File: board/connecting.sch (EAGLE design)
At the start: 14 parts, among them J1 22-05-7038-03, J2 22-05-7038-03, J3 22-05-7038-03, K1 G5L, T1 BC817, X1 External input

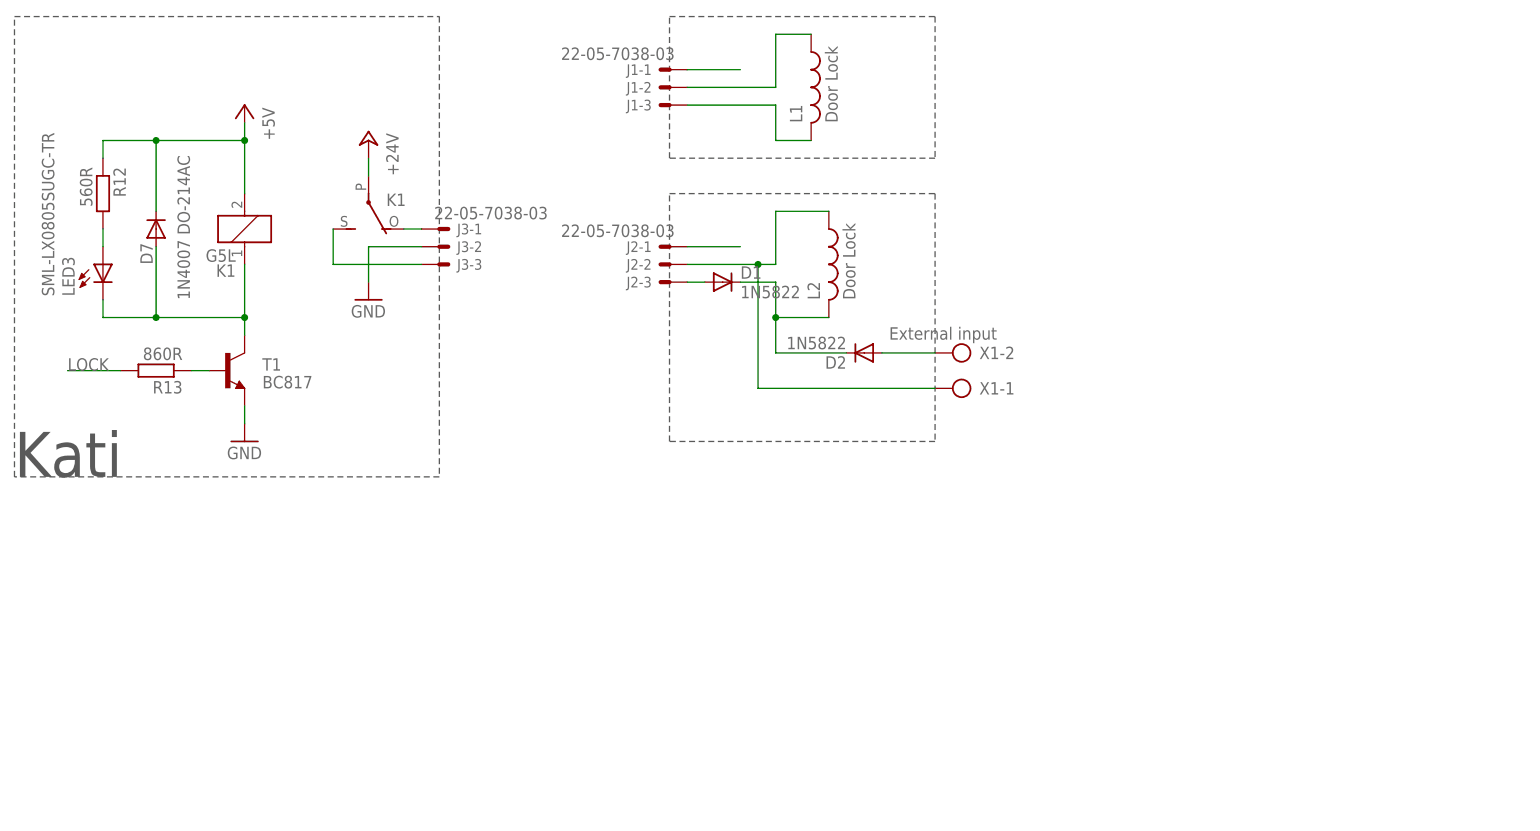
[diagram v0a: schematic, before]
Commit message: Connecting updated
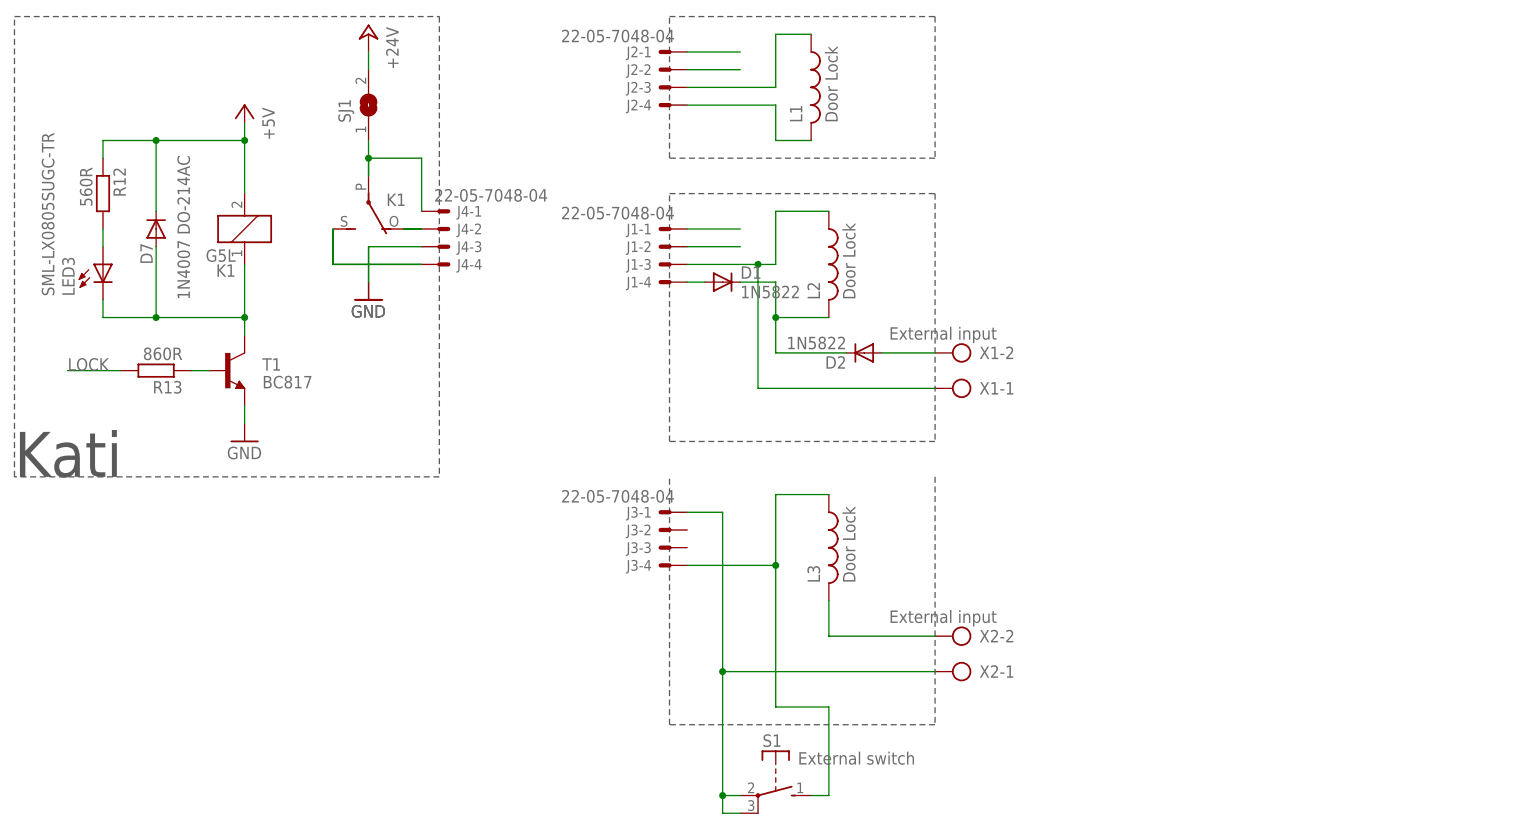
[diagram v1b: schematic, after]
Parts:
- added J4: 22-05-7048-04, con-molex:22-05-7048-04
- added L3: Door Lock, rcl:L-US0204/5
- added S1: External switch, switch-misc:RF15
- added SJ1: (no value), jumper:SJ
- added X2: External input, con-ptr500:AK300/2
- J1, J2, J3: value 22-05-7038-03 -> 22-05-7048-04; device con-molex:22-05-7038-03 -> con-molex:22-05-7048-04
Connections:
- new net C: J4-1.S, SJ1.1
- new net N$14: K12.P
- new net N$20: J3-4.S, L3.1, S1.S
- new net N$21: L3.2, X2-2.KL
- new net N$22: J3-1.S, S1.P, S1.P@1, X2-1.KL
- new net N$3: J2-2.S
- new net N$9: J1-2.S
- new net NC: J4-2.S
- new net NO: J4-4.S
- net +24V: now also SJ1.2; no longer K12.P
- net GND: now also J4-3.S; no longer J3-2.S
- net N$1: now also J2-3.S; no longer J1-2.S
- net N$12: now also J1-4.S; no longer J2-3.S
- net N$2: now also J2-4.S; no longer J1-3.S
- net N$4: now also J1-3.S; no longer J2-2.S
- net N$5: no longer J3-3.S
- net N$7: no longer J3-1.S
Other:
- moved on the sheet: J1-1, J1-2, J1-3, J2-1, J2-2, J2-3, J3-1, J3-2, J3-3

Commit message: Update of connecting diagram, export to image
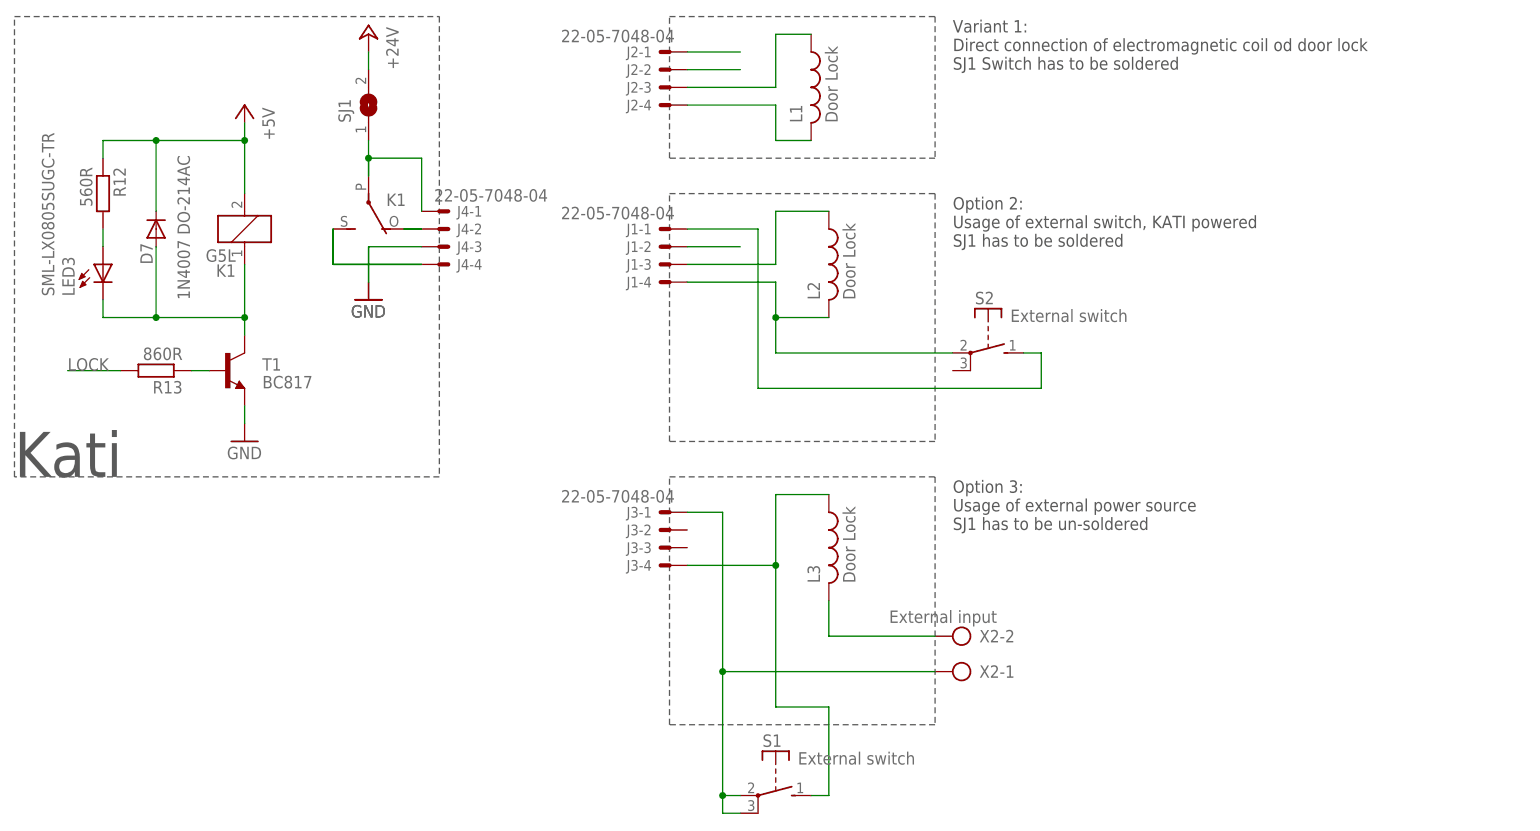
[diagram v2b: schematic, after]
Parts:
- removed D1, D2: 1N5822, diode:1N5059
- removed X1: External input, con-ptr500:AK300/2
- added S2: External switch, switch-misc:RF15
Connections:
- removed net N$12: D1.A, J1-4.S
- removed net N$15: J1-1.S
- net N$13: now also J1-4.S, L2.2, S2.P; no longer D2.A, X1-2.KL
- net N$4: now also J1-1.S, S2.S; no longer J1-3.S, L2.1, X1-1.KL
- net N$6: now also J1-3.S, L2.1; no longer D1.C, D2.C, L2.2
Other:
- note added: "Option 2: Usage of external switch, KATI powered SJ1 has to be soldered"
- note added: "Option 3: Usage of external power source SJ1 has to be un-soldered"
- note added: "Variant 1: Direct connection of electromagnetic coil od door lock SJ1 Switch has to be soldered"
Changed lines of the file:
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@@
 <part name="L1" library="rcl" deviceset="L-US" device="0204/5" value="Door Lock"/>
 <part name="L2" library="rcl" deviceset="L-US" device="0204/5" value="Door Lock"/>
-<part name="D1" library="diode" deviceset="1N5059" device="" value="1N5822"/>
-<part name="D2" library="diode" deviceset="1N5059" device="" value="1N5822"/>
-<part name="X1" library="con-ptr500" deviceset="AK300/2" device="" value="External input"/>
 <part name="GND1" library="supply1" deviceset="GND" device=""/>
 <part name="P+1" library="supply1" deviceset="+24V" device=""/>
@@
 <part name="J3" library="con-molex" deviceset="22-?-04" device="05-7048"/>
 <part name="S1" library="switch-misc" deviceset="RF15" device="" value="External switch"/>
+<part name="S2" library="switch-misc" deviceset="RF15" device="" value="External switch"/>
 </parts>
 <sheets>
@@
 <wire x1="132.08" y1="-15.24" x2="93.98" y2="-15.24" width="0.1524" layer="97" style="shortdash"/>
 <wire x1="93.98" y1="-15.24" x2="93.98" y2="20.32" width="0.1524" layer="97" style="shortdash"/>
+<wire x1="93.98" y1="20.32" x2="132.08" y2="20.32" width="0.1524" layer="97" style="shortdash"/>
+<text x="134.62" y="78.74" size="1.778" layer="97">Variant 1:
+Direct connection of electromagnetic coil od door lock
+SJ1 Switch has to be soldered</text>
+<text x="134.62" y="53.34" size="1.778" layer="97">Option 2:
+Usage of external switch, KATI powered
+SJ1 has to be soldered</text>
+<text x="134.62" y="12.7" size="1.778" layer="97">Option 3:
+Usage of external power source
+SJ1 has to be un-soldered</text>
 </plain>
 <instances>
@@
 <instance part="L1" gate="G$1" x="114.3" y="76.2"/>
 <instance part="L2" gate="G$1" x="116.84" y="50.8"/>
-<instance part="D1" gate="1" x="101.6" y="48.26"/>
-<instance part="D2" gate="1" x="121.92" y="38.1" rot="R180"/>
-<instance part="X1" gate="-1" x="137.16" y="33.02" rot="R180"/>
-<instance part="X1" gate="-2" x="137.16" y="38.1" rot="R180"/>
 <instance part="GND1" gate="1" x="50.8" y="45.72"/>
 <instance part="P+1" gate="1" x="50.8" y="83.82" rot="MR0"/>
@@
 <instance part="J3" gate="-4" x="93.98" y="7.62" rot="MR0"/>
 <instance part="S1" gate="1" x="109.22" y="-25.4" rot="R270"/>
+<instance part="S2" gate="1" x="139.7" y="38.1" rot="R270"/>
 </instances>
 <busses>
@@
 <net name="N$4" class="0">
 <segment>
-<pinref part="L2" gate="G$1" pin="1"/>
-<wire x1="96.52" y1="50.8" x2="106.68" y2="50.8" width="0.1524" layer="91"/>
-<wire x1="106.68" y1="50.8" x2="109.22" y2="50.8" width="0.1524" layer="91"/>
-<wire x1="109.22" y1="50.8" x2="109.22" y2="58.42" width="0.1524" layer="91"/>
-<wire x1="109.22" y1="58.42" x2="116.84" y2="58.42" width="0.1524" layer="91"/>
-<wire x1="106.68" y1="50.8" x2="106.68" y2="33.02" width="0.1524" layer="91"/>
-<junction x="106.68" y="50.8"/>
-<wire x1="106.68" y1="33.02" x2="132.08" y2="33.02" width="0.1524" layer="91"/>
-<pinref part="X1" gate="-1" pin="KL"/>
-<pinref part="J1" gate="-3" pin="S"/>
-</segment>
-</net>
-<net name="N$6" class="0">
-<segment>
+<wire x1="106.68" y1="33.02" x2="147.32" y2="33.02" width="0.1524" layer="91"/>
+<wire x1="147.32" y1="33.02" x2="147.32" y2="38.1" width="0.1524" layer="91"/>
+<pinref part="S2" gate="1" pin="S"/>
+<wire x1="144.78" y1="38.1" x2="147.32" y2="38.1" width="0.1524" layer="91"/>
+<wire x1="106.68" y1="33.02" x2="106.68" y2="55.88" width="0.1524" layer="91"/>
+<pinref part="J1" gate="-1" pin="S"/>
+<wire x1="96.52" y1="55.88" x2="106.68" y2="55.88" width="0.1524" layer="91"/>
+</segment>
+</net>
+<net name="N$9" class="0">
+<segment>
+<wire x1="96.52" y1="53.34" x2="104.14" y2="53.34" width="0.1524" layer="91"/>
+<pinref part="J1" gate="-2" pin="S"/>
+</segment>
+</net>
+<net name="N$13" class="0">
+<segment>
+<pinref part="S2" gate="1" pin="P"/>
 <pinref part="L2" gate="G$1" pin="2"/>
 <wire x1="116.84" y1="43.18" x2="109.22" y2="43.18" width="0.1524" layer="91"/>
 <wire x1="109.22" y1="43.18" x2="109.22" y2="48.26" width="0.1524" layer="91"/>
-<wire x1="109.22" y1="48.26" x2="104.14" y2="48.26" width="0.1524" layer="91"/>
-<pinref part="D1" gate="1" pin="C"/>
-<pinref part="D2" gate="1" pin="C"/>
-<wire x1="119.38" y1="38.1" x2="109.22" y2="38.1" width="0.1524" layer="91"/>
+<wire x1="134.62" y1="38.1" x2="109.22" y2="38.1" width="0.1524" layer="91"/>
 <wire x1="109.22" y1="38.1" x2="109.22" y2="43.18" width="0.1524" layer="91"/>
 <junction x="109.22" y="43.18"/>
-</segment>
-</net>
-<net name="N$9" class="0">
-<segment>
-<wire x1="96.52" y1="53.34" x2="104.14" y2="53.34" width="0.1524" layer="91"/>
-<pinref part="J1" gate="-2" pin="S"/>
-</segment>
-</net>
-<net name="N$12" class="0">
-<segment>
-<pinref part="D1" gate="1" pin="A"/>
-<wire x1="99.06" y1="48.26" x2="96.52" y2="48.26" width="0.1524" layer="91"/>
 <pinref part="J1" gate="-4" pin="S"/>
-</segment>
-</net>
-<net name="N$13" class="0">
-<segment>
-<pinref part="D2" gate="1" pin="A"/>
-<wire x1="124.46" y1="38.1" x2="132.08" y2="38.1" width="0.1524" layer="91"/>
-<pinref part="X1" gate="-2" pin="KL"/>
+<wire x1="109.22" y1="48.26" x2="96.52" y2="48.26" width="0.1524" layer="91"/>
 </segment>
 </net>
@@
 <pinref part="K1" gate="2" pin="P"/>
 <wire x1="50.8" y1="66.04" x2="50.8" y2="63.5" width="0.1524" layer="91"/>
-</segment>
-</net>
-<net name="N$15" class="0">
-<segment>
-<pinref part="J1" gate="-1" pin="S"/>
-<wire x1="96.52" y1="55.88" x2="104.14" y2="55.88" width="0.1524" layer="91"/>
 </segment>
 </net>
@@
 </segment>
 </net>
+<net name="N$6" class="0">
+<segment>
+<pinref part="L2" gate="G$1" pin="1"/>
+<wire x1="109.22" y1="58.42" x2="116.84" y2="58.42" width="0.1524" layer="91"/>
+<wire x1="109.22" y1="50.8" x2="109.22" y2="58.42" width="0.1524" layer="91"/>
+<wire x1="96.52" y1="50.8" x2="109.22" y2="50.8" width="0.1524" layer="91"/>
+<pinref part="J1" gate="-3" pin="S"/>
+</segment>
+</net>
 </nets>
 </sheet>
@@
 </schematic>
 </drawing>
+<compatibility>
+<note version="6.3" minversion="6.2.2" severity="warning">
+Since Version 6.2.2 text objects can contain more than one line,
+which will not be processed correctly with this version.
+</note>
+</compatibility>
 </eagle>
